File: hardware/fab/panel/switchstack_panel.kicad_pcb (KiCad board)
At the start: 2 copper layers, 173.4 x 64.4 mm, 230 parts

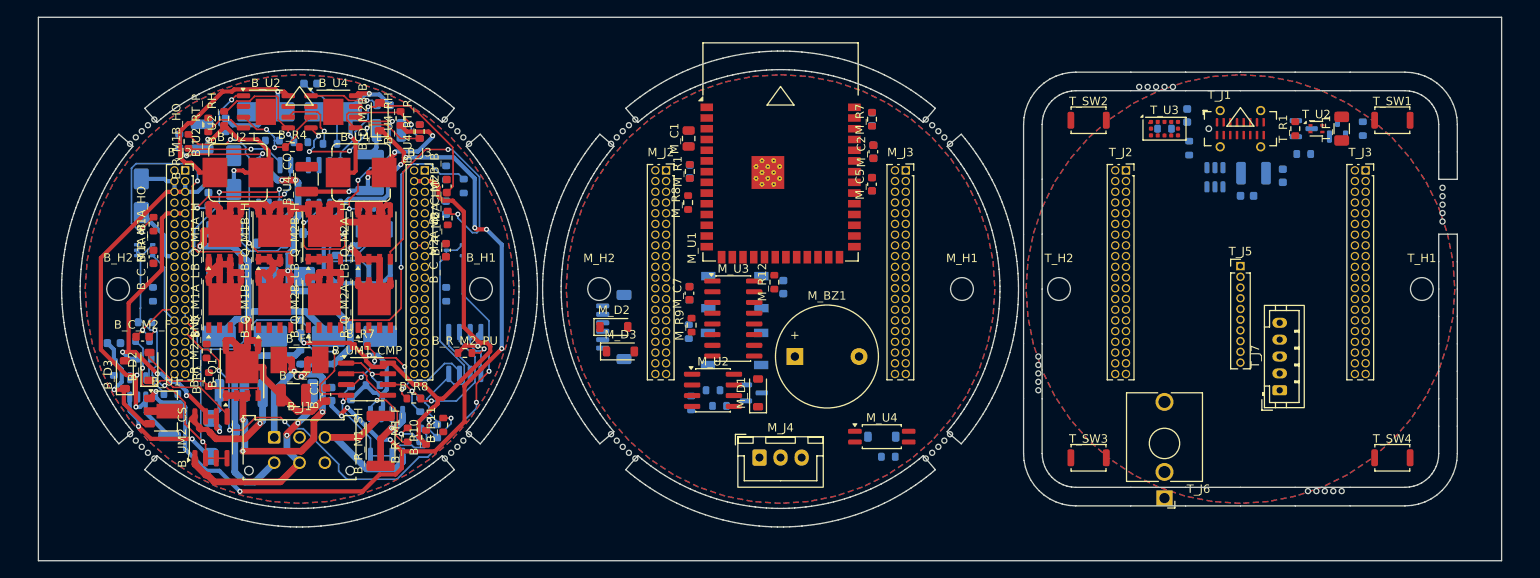
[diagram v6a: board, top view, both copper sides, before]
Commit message: Adapter mit USB-Freistellung, Nutzen vierlagig
ADAPTER. Die USB-Buchse steht auf Mid und greift durch die Randkerbe des
Top-Boards - ihr Koerper reicht bis y = 22,45, die zentrale Durchfuehrung des
Adapters endete aber bei 21,5. Ohne Freistellung waere die Buchse gegen den
Auflagesteg gestossen. Die Durchfuehrung ist an dieser Stelle jetzt bis
y = 24,0 verlaengert, also bis hinter die Boardkante.

Damit ist der Adapter nicht mehr punktsymmetrisch: y waechst wie in KiCad
nach unten, zur 6-Uhr-Seite, wo Klinkenbuchse, USB-Kerbe und Freistellung
liegen. Die Kerbe des Top-Boards zeigt in dieselbe Richtung und macht die
Einbaulage beim Zusammenbau sichtbar. Drei neue Selbsttests pruefen, dass die
Freistellung den Buchsenkoerper abdeckt und nicht mehr als 30 % der
Auflagekante wegnimmt. Selbsttest bestanden.

NUTZEN. Er war noch zweilagig, waehrend die Quellboards vier Lagen haben -
alle Bahnen auf In1/In2 lagen damit auf einer abgeschalteten Lage:

  vorher    item_on_disabled_layer 199, track_dangling 199, via_dangling 152,
            unconnected_items 499, isolated_copper 6
  jetzt     alles davon null

Dazu bekommt der Nutzen die .kicad_dru der Einzelprojekte - sonst prueft er
die Befestigungsloecher der Steckverbinder wieder gegen die 0,5-mm-
Kantenregel (hole_clearance 27, shorting_items 1; beide jetzt null).

Der Nutzen ist damit deckungsgleich mit der Summe der Einzelboards:
clearance 1, copper_edge_clearance 1, unconnected_items 55 - genau
4 + 21 + 30 aus Top, Mid und Bottom.

Co-Authored-By: Claude Opus 5 (1M context) <noreply@anthropic.com>
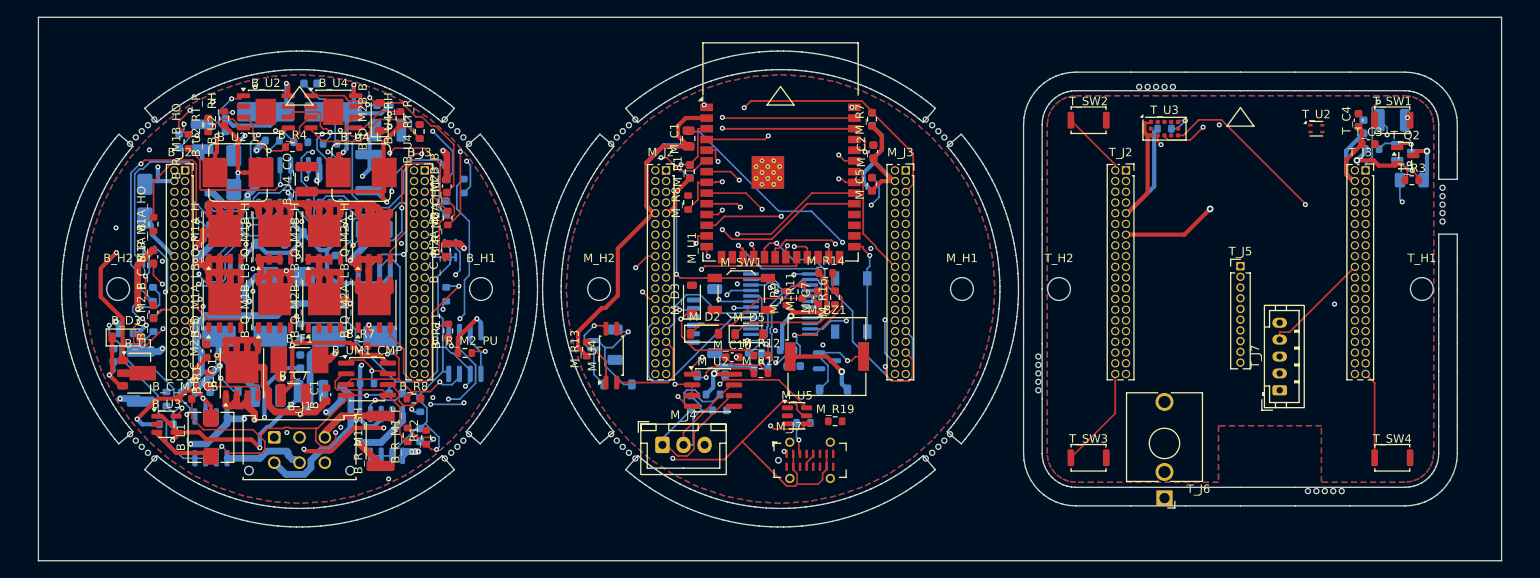
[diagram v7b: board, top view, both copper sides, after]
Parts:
- removed T_J1: USB-C, USB_C_Receptacle_G-Switch_GT-USB-7051x
- removed T_R1, T_R2: 5k1, R_0603_1608Metric
- removed T_U1: USBLC6-2SC6, SOT-23-6
- added M_C10: 100n, C_0603_1608Metric, F.Cu at (-4.48, 8.08)
- added M_C9: 100n, C_0603_1608Metric, B.Cu at (2.81, 9.14)
- added M_D5: 5V6, D_SOD-123, F.Cu at (-2.47, 5.35)
- added M_D6: 5V6, D_SOD-123, B.Cu at (-6.97, 10.3)
- added M_J6: Haubenkontakt, JST_SH_BM02B-SRSS-TB_1x02-1MP_P1.00mm_Vertical, B.Cu at (-19.6, 6.60)
- added M_J7: USB-C, USB_C_Receptacle_G-Switch_GT-USB-7051x, F.Cu at (4.75, 20.3)
- added M_R14: 10k, R_0603_1608Metric, F.Cu at (6.60, -1.89)
- added M_R15: 10k, R_0603_1608Metric, B.Cu at (-1.07, 9.46)
- added M_R16: 1k, R_0603_1608Metric, F.Cu at (7.70, 1.02)
- added M_R17: 1k, R_0603_1608Metric, F.Cu at (-1.08, 9.98)
- added M_R18: 5k1, R_0603_1608Metric, B.Cu at (3.97, 15.9)
- added M_R19: 5k1, R_0603_1608Metric, F.Cu at (7.72, 15.7)
- added M_U5: USBLC6-2SC6, SOT-23-6, F.Cu at (3.20, 15.0)
- B_C2, B_D2, B_R10, B_R_M2_LNK, B_UM2_CS, M_D1, T_F1: moved to B.Cu
- B_C7, B_C_M1_CS, B_C_M2_CS, B_L1, B_R12, B_U3, M_R11, M_R13, M_SW1, T_C3, T_C4, T_Q2, T_R3: moved to F.Cu
- M_BZ1: value Piezo passiv -> Piezo passiv SMD; footprint Buzzer_12x9.5RM7.6 -> Buzzer_Murata_PKMCS0909E
- M_J5: value Feld: Reed 1/2, Haube -> Feld: 4 Reed
- M_U3: value PCF8574 -> PCF8575; footprint SOIC-16_3.9x9.9mm_P1.27mm -> SSOP-24_5.3x8.2mm_P0.65mm; moved to B.Cu
- moved M_R13 37.9 mm to (-21.7, 7.12), turned to 90 degrees
- moved B_R12 36.0 mm to (-40.8, 17.6), turned to 90 degrees
- moved M_U4 33.5 mm to (-18.8, 7.90), turned to 90 degrees
- moved M_D4 31.9 mm to (-18.0, 11.3)
- moved T_C1 20.9 mm to (70.3, -19.2)
- moved B_C_M1_CS 19.7 mm to (-69.3, 13.0), turned to 0 degrees
- moved B_R10 19.5 mm to (-55.6, 4.96)
- moved T_C2 17.6 mm to (73.8, -20.0)
- moved B_R_M2_SH 17.5 mm to (-74.6, 10.4), turned to 90 degrees
- moved B_C8 17.2 mm to (-54.4, 12.1), turned to 0 degrees
- moved T_C4 16.0 mm to (69.8, -20.0), turned to 90 degrees
- moved M_C7 15.2 mm to (5.68, 1.02)
- moved M_SW2 14.8 mm to (9.62, 1.89), turned to 90 degrees
- moved M_R11 14.3 mm to (3.85, 0.30)
- moved M_R10 13.4 mm to (2.03, 7.24), turned to 0 degrees
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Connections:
- net BOT_RADAR_INT renamed BOT_PRESENCE_INT
- net BOT_UART_RADAR_RX renamed BOT_UART_AUX_RX
- net BOT_UART_RADAR_TX renamed BOT_UART_AUX_TX
- net BOT_USB_DN renamed BOT_RSV_A5
- net BOT_USB_DP renamed BOT_RSV_A3
- B_J2 pad 2: BOT_PGND -> BOT_BTN2
- B_J2 pad 40: BOT_PGND -> BOT_BTN3
- B_J3 pad 1: BOT_PGND -> BOT_BTN1
- B_J3 pad 26: BOT_BTN1 -> BOT_PGND
- B_J3 pad 27: BOT_BTN2 -> BOT_PGND
- B_J3 pad 28: BOT_BTN3 -> BOT_PGND
- B_J3 pad 29: BOT_BTN4 -> BOT_PGND
- B_J3 pad 39: BOT_PGND -> BOT_BTN4
- B_J3 pad 5: BOT_PGND -> BOT_I2C_SCL
- B_J3 pad 6: BOT_I2C_SCL -> BOT_PGND
- B_J3 pad 7: BOT_PGND -> BOT_I2C_SDA
- B_J3 pad 8: BOT_I2C_SDA -> BOT_PGND
- M_J2 pad 2: MID_PGND -> MID_BTN2
- M_J2 pad 34: MID_USB_DP -> MID_RSV_A3
- M_J2 pad 36: MID_USB_DN -> MID_RSV_A5
- M_J2 pad 40: MID_PGND -> MID_BTN3
- M_J3 pad 1: MID_PGND -> MID_BTN1
- M_J3 pad 26: MID_BTN1 -> MID_PGND
- M_J3 pad 27: MID_BTN2 -> MID_PGND
- M_J3 pad 28: MID_BTN3 -> MID_PGND
- M_J3 pad 29: MID_BTN4 -> MID_PGND
- M_J3 pad 39: MID_PGND -> MID_BTN4
- M_J3 pad 5: MID_PGND -> MID_I2C_SCL
- M_J3 pad 6: MID_I2C_SCL -> MID_PGND
- M_J3 pad 7: MID_PGND -> MID_I2C_SDA
- M_J3 pad 8: MID_I2C_SDA -> MID_PGND
- M_J5 pad 2: MID_PGND -> MID_SAB1_IN
- M_J5 pad 3: MID_REED2_IN -> MID_PGND
- M_J5 pad 4: MID_PGND -> MID_REED2_IN
- M_J5 pad 5: MID_HOOD_A -> MID_SAB2_IN
- M_J5 pad 6: MID_HOOD_B -> MID_PGND
- M_U3 pad 1: MID_PGND -> (no net)
- M_U3 pad 10: MID_RELAY_CTL -> MID_EXP_P6
- M_U3 pad 11: MID_EXP_P6 -> MID_EXP_P7
- M_U3 pad 12: MID_EXP_P7 -> MID_PGND
- M_U3 pad 13: (no net) -> MID_EXP_P8
- M_U3 pad 14: MID_I2C_SCL -> MID_EXP_P9
- M_U3 pad 15: MID_I2C_SDA -> (no net)
- M_U3 pad 16: MID_3V3_SYS -> (no net)
- M_U3 pad 8: MID_PGND -> MID_PRESENCE_INT
- M_U3 pad 9: MID_PRESENCE_INT -> MID_RELAY_CTL
- T_J2 pad 2: TOP_PGND -> TOP_BTN2
- T_J2 pad 34: TOP_USB_DP -> TOP_RSV_A3
- T_J2 pad 36: TOP_USB_DN -> TOP_RSV_A5
- T_J2 pad 40: TOP_PGND -> TOP_BTN3
- T_J3 pad 1: TOP_PGND -> TOP_BTN1
- T_J3 pad 26: TOP_BTN1 -> TOP_PGND
- T_J3 pad 27: TOP_BTN2 -> TOP_PGND
- T_J3 pad 28: TOP_BTN3 -> TOP_PGND
- T_J3 pad 29: TOP_BTN4 -> TOP_PGND
- T_J3 pad 39: TOP_PGND -> TOP_BTN4
- T_J3 pad 5: TOP_PGND -> TOP_I2C_SCL
- T_J3 pad 6: TOP_I2C_SCL -> TOP_PGND
- T_J3 pad 7: TOP_PGND -> TOP_I2C_SDA
- T_J3 pad 8: TOP_I2C_SDA -> TOP_PGND
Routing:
- net MID_3V3_SYS: track 0.00 -> 177.2 mm, vias 0 -> 2
- net BOT_M2_INA: track 0.00 -> 124.0 mm, vias 0 -> 5
- net TOP_3V3_SYS: track 0.00 -> 94.5 mm
- net BOT_M1_SWA: track 23.9 -> 113.7 mm, vias 1 -> 3
- net BOT_M2_SWA: track 32.5 -> 109.2 mm, vias 2 -> 6
- net BOT_M2_SWB: track 14.0 -> 85.6 mm, vias 0 -> 3
- net TOP_PRESENCE_INT: track 0.00 -> 67.2 mm, vias 0 -> 1
- net MID_I2C_SCL: track 0.00 -> 67.1 mm, vias 0 -> 2
- net MID_USB_VBUS: track 0.00 -> 66.0 mm, vias 0 -> 2
- net MID_I2C_SDA: track 0.00 -> 63.9 mm, vias 0 -> 3
- net BOT_TRIP_RST: track 0.00 -> 59.4 mm, vias 0 -> 1
- net BOT_24V_PROT: track 110.5 -> 165.3 mm, vias 2 -> 5
- net MID_AUDIO_PWM: track 0.00 -> 54.2 mm, vias 0 -> 1
- net TOP_STAR_OUT: track 0.00 -> 54.1 mm, vias 0 -> 1
- net MID_UART485_TX: track 0.00 -> 53.9 mm, vias 0 -> 3
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- added copper zone on In1.Cu, net BOT_PGND
- added copper zone on In2.Cu, net BOT_PGND
- added copper zone on In1.Cu, net MID_PGND
- added copper zone on In2.Cu, net MID_PGND
- added copper zone on In1.Cu, net TOP_PGND
- added copper zone on In2.Cu, net TOP_PGND
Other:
- copper layers 2 -> 4
